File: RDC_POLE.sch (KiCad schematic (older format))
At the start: 36 parts, among them J2 RESOLVER POLE, Q3 BC807, Q4 BC807, U2 AD8397ARZ, X2 8.192MHz

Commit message: agrandados pads de test points
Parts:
- TP10, TP11, TP12, TP13, TP14, TP15: footprint TestPoint:TestPoint_THTPad_1.5x1.5mm_Drill0.7mm -> TestPoint:TestPoint_reducido
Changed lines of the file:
@@
 F 0 "TP14" V 9904 3138 50  0000 L CNN
 F 1 "TPEXCPOLE" V 9995 3138 50  0000 L CNN
-F 2 "TestPoint:TestPoint_THTPad_1.5x1.5mm_Drill0.7mm" H 10150 2950 50  0001 C CNN
+F 2 "TestPoint:TestPoint_reducido" H 10150 2950 50  0001 C CNN
 F 3 "~" H 10150 2950 50  0001 C CNN
 	1    9950 2950
@@
 F 0 "TP15" V 9904 5638 50  0000 L CNN
 F 1 "TPEXCLOPOLE" V 9995 5638 50  0000 L CNN
-F 2 "TestPoint:TestPoint_THTPad_1.5x1.5mm_Drill0.7mm" H 10150 5450 50  0001 C CNN
+F 2 "TestPoint:TestPoint_reducido" H 10150 5450 50  0001 C CNN
 F 3 "~" H 10150 5450 50  0001 C CNN
 	1    9950 5450
@@
 F 0 "TP10" V 3300 2600 50  0000 L CNN
 F 1 "TPCOSPOLE" V 3350 2900 50  0000 L CNN
-F 2 "TestPoint:TestPoint_THTPad_1.5x1.5mm_Drill0.7mm" H 3550 2700 50  0001 C CNN
+F 2 "TestPoint:TestPoint_reducido" H 3550 2700 50  0001 C CNN
 F 3 "~" H 3550 2700 50  0001 C CNN
 	1    3350 2700
@@
 F 0 "TP11" V 3400 2600 50  0000 L CNN
 F 1 "TPCOSLOPOLE" V 3450 2900 50  0000 L CNN
-F 2 "TestPoint:TestPoint_THTPad_1.5x1.5mm_Drill0.7mm" H 3650 2700 50  0001 C CNN
+F 2 "TestPoint:TestPoint_reducido" H 3650 2700 50  0001 C CNN
 F 3 "~" H 3650 2700 50  0001 C CNN
 	1    3450 2700
@@
 F 0 "TP12" V 3600 2600 50  0000 L CNN
 F 1 "TPSINLOPOLE" V 3650 2900 50  0000 L CNN
-F 2 "TestPoint:TestPoint_THTPad_1.5x1.5mm_Drill0.7mm" H 3850 2700 50  0001 C CNN
+F 2 "TestPoint:TestPoint_reducido" H 3850 2700 50  0001 C CNN
 F 3 "~" H 3850 2700 50  0001 C CNN
 	1    3650 2700
@@
 F 0 "TP13" V 3700 2600 50  0000 L CNN
 F 1 "TPSINPOLE" V 3750 2900 50  0000 L CNN
-F 2 "TestPoint:TestPoint_THTPad_1.5x1.5mm_Drill0.7mm" H 3950 2700 50  0001 C CNN
+F 2 "TestPoint:TestPoint_reducido" H 3950 2700 50  0001 C CNN
 F 3 "~" H 3950 2700 50  0001 C CNN
 	1    3750 2700

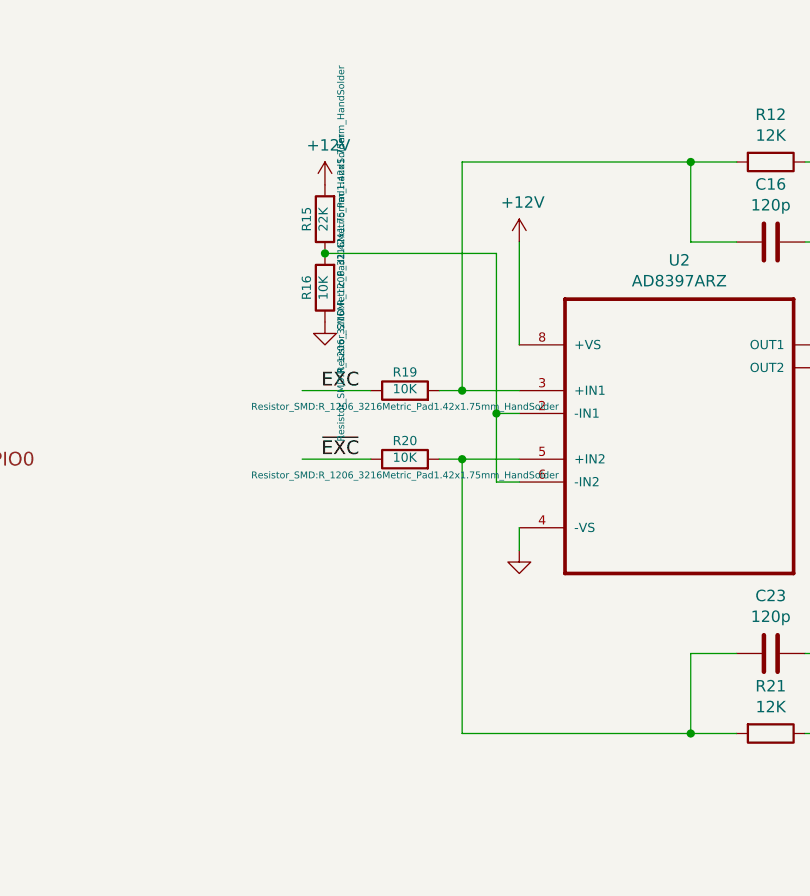
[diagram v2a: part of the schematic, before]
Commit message: Se arregló conexion erronea en los amplificadores operacionales
se agregó conexión 1-wire en GPIO8
se agregó botón y led que comparten GPIO7, la idea es leer el estado del
botón y al liberarlo cambiar el GPIO a output y encender el led indicando
alguna acción
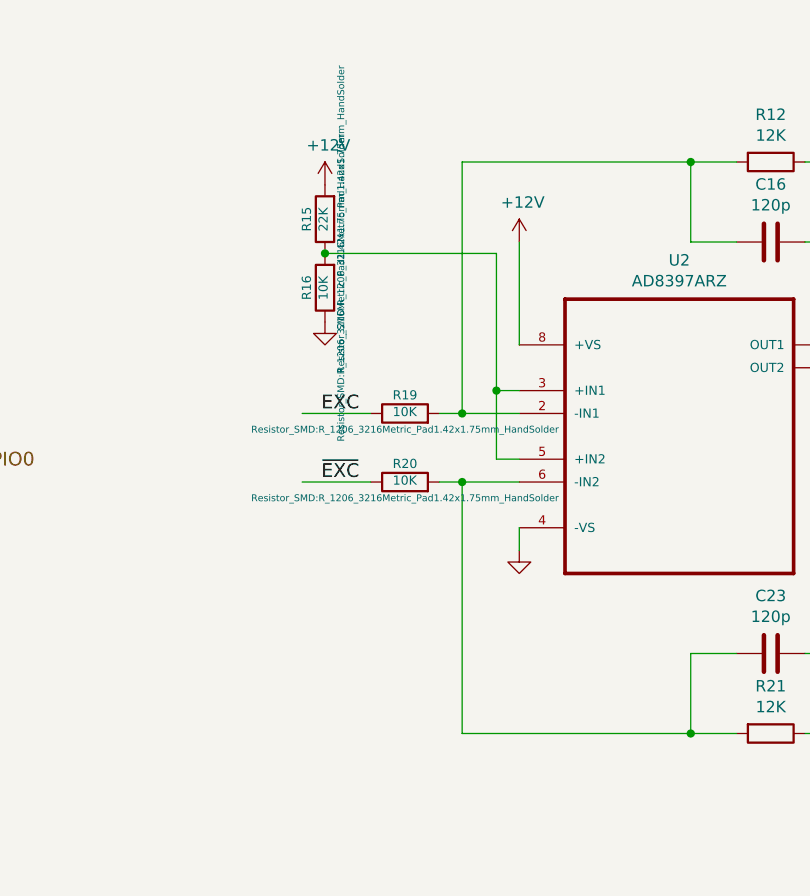
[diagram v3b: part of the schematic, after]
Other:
- moved on the sheet: R19, R20
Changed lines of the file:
@@
 Wire Wire Line
 	8550 4550 8550 4650
-Text Label 7850 4250 2    60   ~ 0
-~EXC
-Wire Wire Line
-	8450 4350 8550 4350
 Wire Wire Line
 	7700 3350 8450 3350
@@
 	9950 5450 9800 5450
 Wire Wire Line
-	8300 4250 8550 4250
-Wire Wire Line
 	4750 2050 5100 2050
 Connection ~ 4750 2050
 Text Label 5050 2050 2    60   ~ 0
 AGND
-$Comp
-L Device:R R?
-U 1 1 5EFA85F8
-P 8050 4250
-AR Path="/5EFA85F8" Ref="R?"  Part="1"
-AR Path="/5EF45E27/5EFA85F8" Ref="R?"  Part="1"
-AR Path="/5F077C82/5EFA85F8" Ref="R20"  Part="1"
-F 0 "R20" V 8130 4250 40  0000 C CNN
-F 1 "10K" V 8057 4251 40  0000 C CNN
-F 2 "Resistor_SMD:R_1206_3216Metric_Pad1.42x1.75mm_HandSolder" V 7980 4250 30  0000 C CNN
-F 3 "~" H 8050 4250 30  0000 C CNN
-	1    8050 4250
-	0    -1   -1   0
-$EndComp
-$Comp
-L Device:R R?
-U 1 1 5EFA85FE
-P 8050 3950
-AR Path="/5EFA85FE" Ref="R?"  Part="1"
-AR Path="/5EF45E27/5EFA85FE" Ref="R?"  Part="1"
-AR Path="/5F077C82/5EFA85FE" Ref="R19"  Part="1"
-F 0 "R19" V 8130 3950 40  0000 C CNN
-F 1 "10K" V 8057 3951 40  0000 C CNN
-F 2 "Resistor_SMD:R_1206_3216Metric_Pad1.42x1.75mm_HandSolder" V 7980 3950 30  0000 C CNN
-F 3 "~" H 8050 3950 30  0000 C CNN
-	1    8050 3950
-	0    -1   -1   0
-$EndComp
 Wire Wire Line
 	8550 3300 8550 3750
-Wire Wire Line
-	8200 3950 8300 3950
-Connection ~ 8300 3950
-Wire Wire Line
-	8200 4250 8300 4250
-Connection ~ 8300 4250
-Wire Wire Line
-	7600 3950 7900 3950
-Wire Wire Line
-	7900 4250 7600 4250
 Text Label 10500 4550 2    60   ~ 0
 AGND
@@
 Connection ~ 9300 5450
 Wire Wire Line
-	8300 4250 8300 5450
-Wire Wire Line
 	9500 5100 9300 5100
 Wire Wire Line
@@
 Text Notes 4450 2700 0    60   ~ 0
 A0/A1\n 0  0 Normal mode—position output\n 0  1 Normal mode—velocity output\n 1  0 Reserved\n 1  1 Configuration mode
-Connection ~ 8450 4050
-Wire Wire Line
-	8450 4050 8450 4350
-Wire Wire Line
-	8450 4050 8550 4050
-Wire Wire Line
-	8300 2950 8300 3950
-Wire Wire Line
-	8300 3950 8550 3950
-Wire Wire Line
-	8450 3350 8450 4050
-Text Label 7850 3950 2    60   ~ 0
-EXC
 Wire Wire Line
 	2050 4050 2600 4050
@@
 Text Label 10500 4250 2    60   ~ 0
 AGND
+Text Label 7850 4050 2    60   ~ 0
+EXC
+Wire Wire Line
+	8300 4050 8550 4050
+Wire Wire Line
+	8300 4350 8300 5450
+Wire Wire Line
+	7900 4350 7600 4350
+Wire Wire Line
+	7600 4050 7900 4050
+Connection ~ 8300 4350
+Wire Wire Line
+	8200 4350 8300 4350
+Connection ~ 8300 4050
+Wire Wire Line
+	8200 4050 8300 4050
+$Comp
+L Device:R R?
+U 1 1 5EFA85FE
+P 8050 4050
+AR Path="/5EFA85FE" Ref="R?"  Part="1"
+AR Path="/5EF45E27/5EFA85FE" Ref="R?"  Part="1"
+AR Path="/5F077C82/5EFA85FE" Ref="R19"  Part="1"
+F 0 "R19" V 8130 4050 40  0000 C CNN
+F 1 "10K" V 8057 4051 40  0000 C CNN
+F 2 "Resistor_SMD:R_1206_3216Metric_Pad1.42x1.75mm_HandSolder" V 7980 4050 30  0000 C CNN
+F 3 "~" H 8050 4050 30  0000 C CNN
+	1    8050 4050
+	0    -1   -1   0
+$EndComp
+$Comp
+L Device:R R?
+U 1 1 5EFA85F8
+P 8050 4350
+AR Path="/5EFA85F8" Ref="R?"  Part="1"
+AR Path="/5EF45E27/5EFA85F8" Ref="R?"  Part="1"
+AR Path="/5F077C82/5EFA85F8" Ref="R20"  Part="1"
+F 0 "R20" V 8130 4350 40  0000 C CNN
+F 1 "10K" V 8057 4351 40  0000 C CNN
+F 2 "Resistor_SMD:R_1206_3216Metric_Pad1.42x1.75mm_HandSolder" V 7980 4350 30  0000 C CNN
+F 3 "~" H 8050 4350 30  0000 C CNN
+	1    8050 4350
+	0    -1   -1   0
+$EndComp
+Wire Wire Line
+	8300 4350 8550 4350
+Wire Wire Line
+	8450 4250 8550 4250
+Text Label 7850 4350 2    60   ~ 0
+~EXC
+Wire Wire Line
+	8450 3350 8450 3950
+Wire Wire Line
+	8550 3950 8450 3950
+Connection ~ 8450 3950
+Wire Wire Line
+	8450 3950 8450 4250
+Wire Wire Line
+	8300 2950 8300 4050
 $EndSCHEMATC
